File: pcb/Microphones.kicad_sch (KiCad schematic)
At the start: 40 parts, among them J14 Conn_02x01, U1 AD8426ACPZ-R7, U2 AD8426ACPZ-R7, U3 LT1790ACS6-1.25

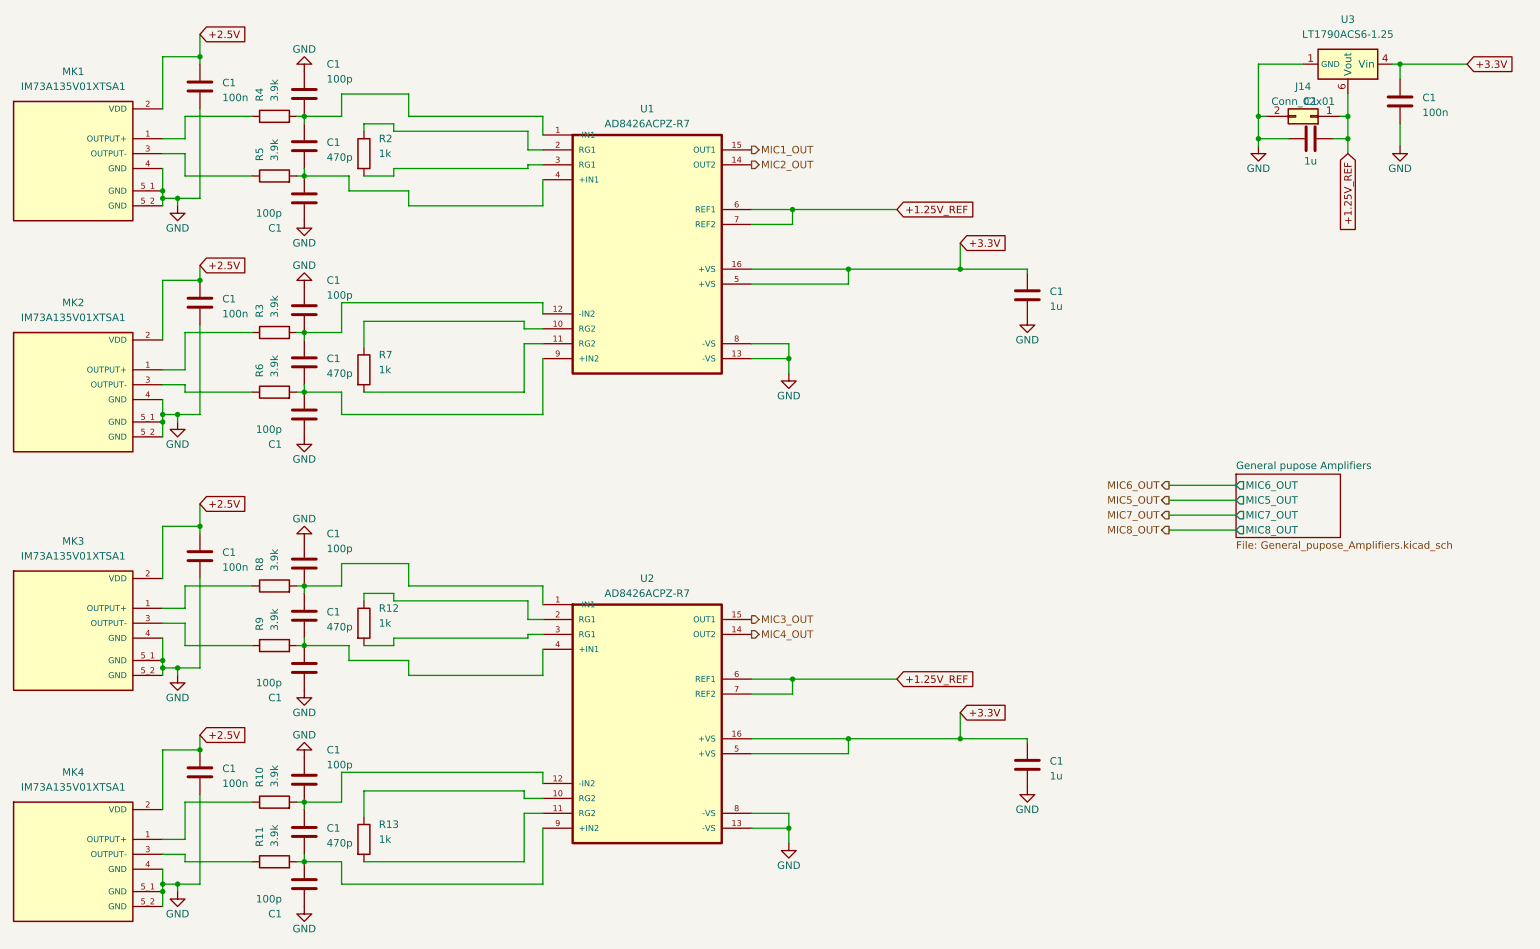
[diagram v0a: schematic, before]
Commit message: feat: Reorganize PCB project
Include all 3D step files
Refactor all folders for symbolds and footprints
Add missing datasheets
Link all symbols in KiCad projects
Rename the project to SensEdu
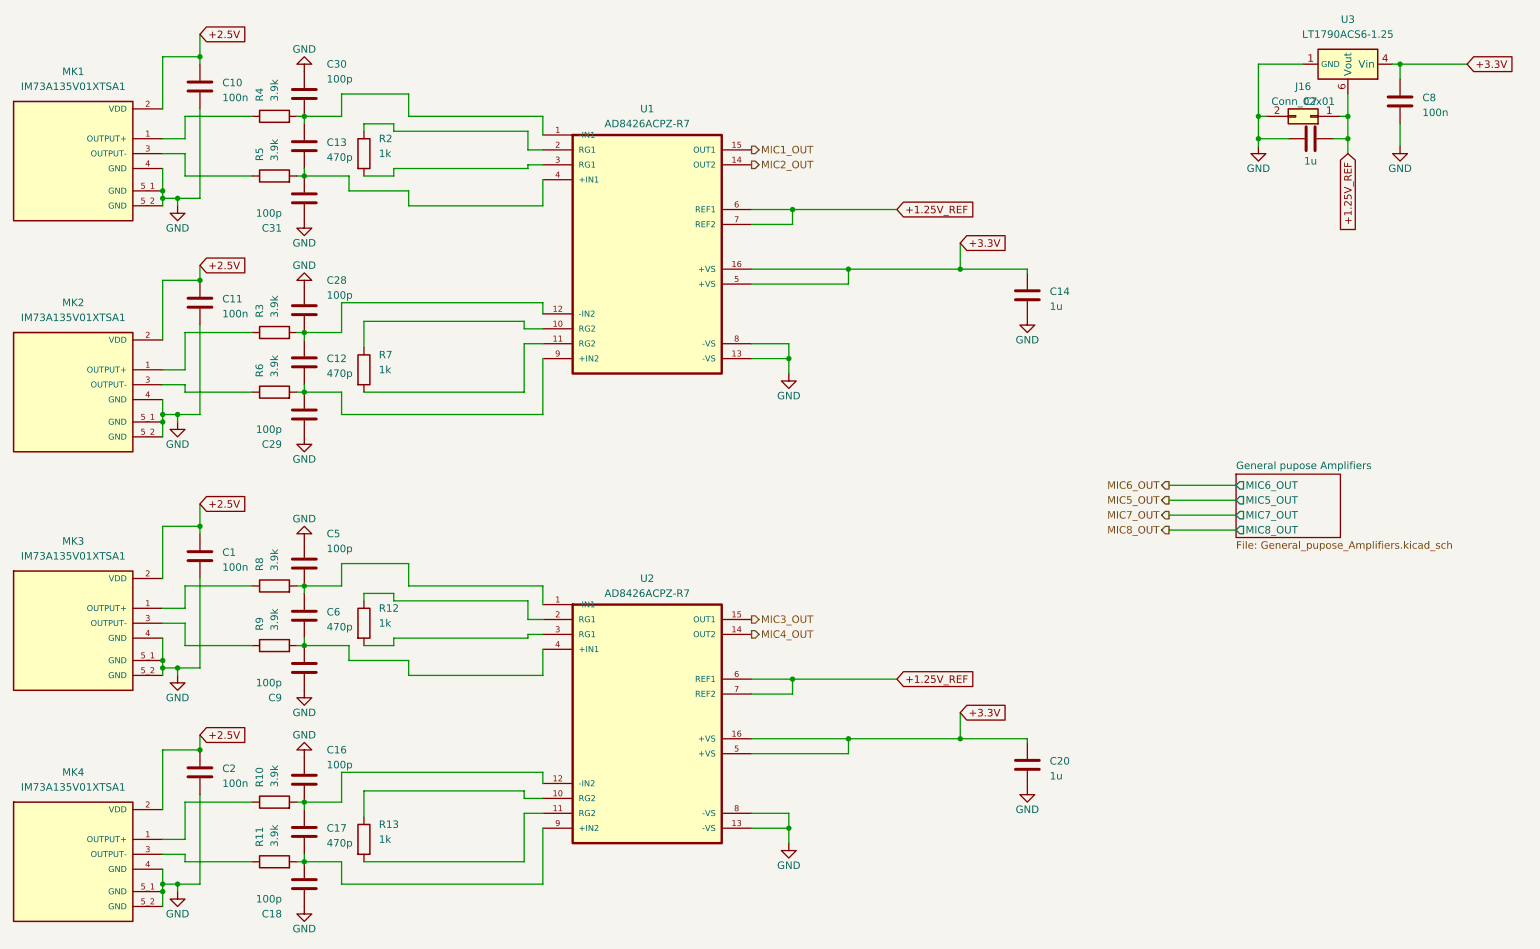
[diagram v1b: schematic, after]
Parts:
- renumbered C1 to C10, C1 to C11, C1 to C12, C1 to C13, C1 to C14, C1 to C16, C1 to C17, C1 to C18, C1 to C2, C1 to C20, C1 to C28, C1 to C29, C1 to C30, C1 to C31, C1 to C5, C1 to C6, C1 to C7, C1 to C8, C1 to C9, J14 to J16

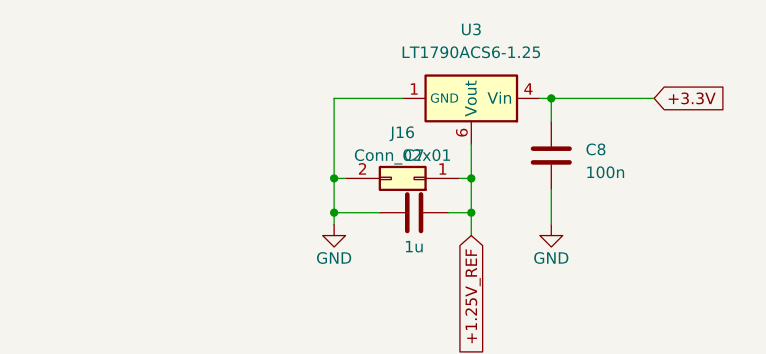
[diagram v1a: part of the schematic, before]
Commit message: feat: Fix DRC errors and warnings
Updated footprint links
Updated schematic symbol for LT1790 to remove warnings
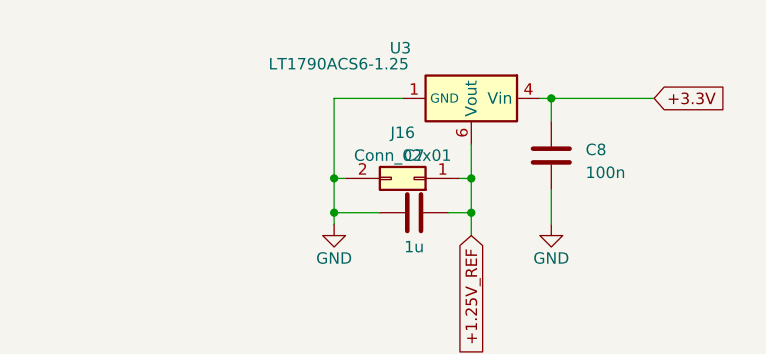
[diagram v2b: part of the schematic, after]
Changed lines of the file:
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@@
 		(on_board yes)
 		(dnp no)
-		(fields_autoplaced yes)
 		(property "Reference" "U3"
-			(at 254 15.24 90)
+			(at 246.126 17.272 90)
 			(effects
 				(font
@@
 		)
 		(property "Value" "LT1790ACS6-1.25"
-			(at 254 17.78 90)
+			(at 239.268 19.05 90)
 			(effects
 				(font
@@
 		(pin "6"
 		)
+		(pin "5"
+		)
+		(pin "3"
+		)
 		(instances
